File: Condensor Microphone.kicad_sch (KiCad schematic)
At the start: 13 parts, among them J16 Conn_01x02, U2 MAX4466EXK_T

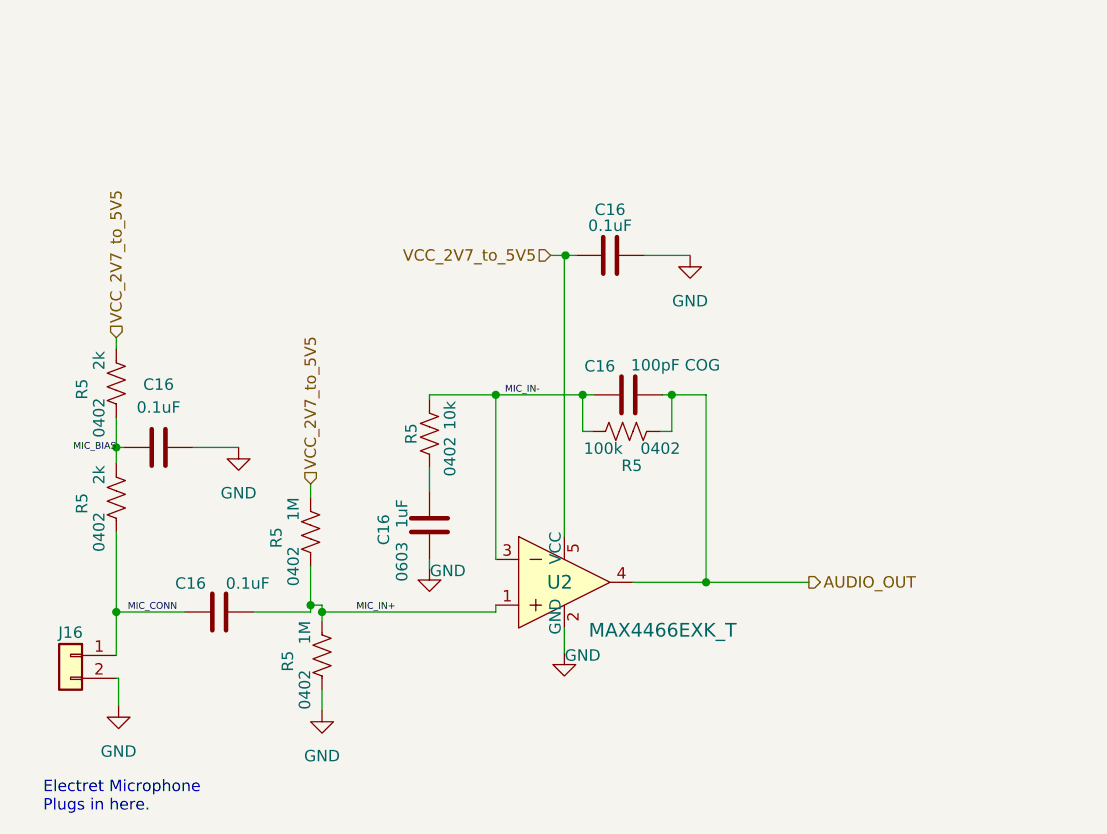
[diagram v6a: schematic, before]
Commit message: updated parts with those available on jlpcb
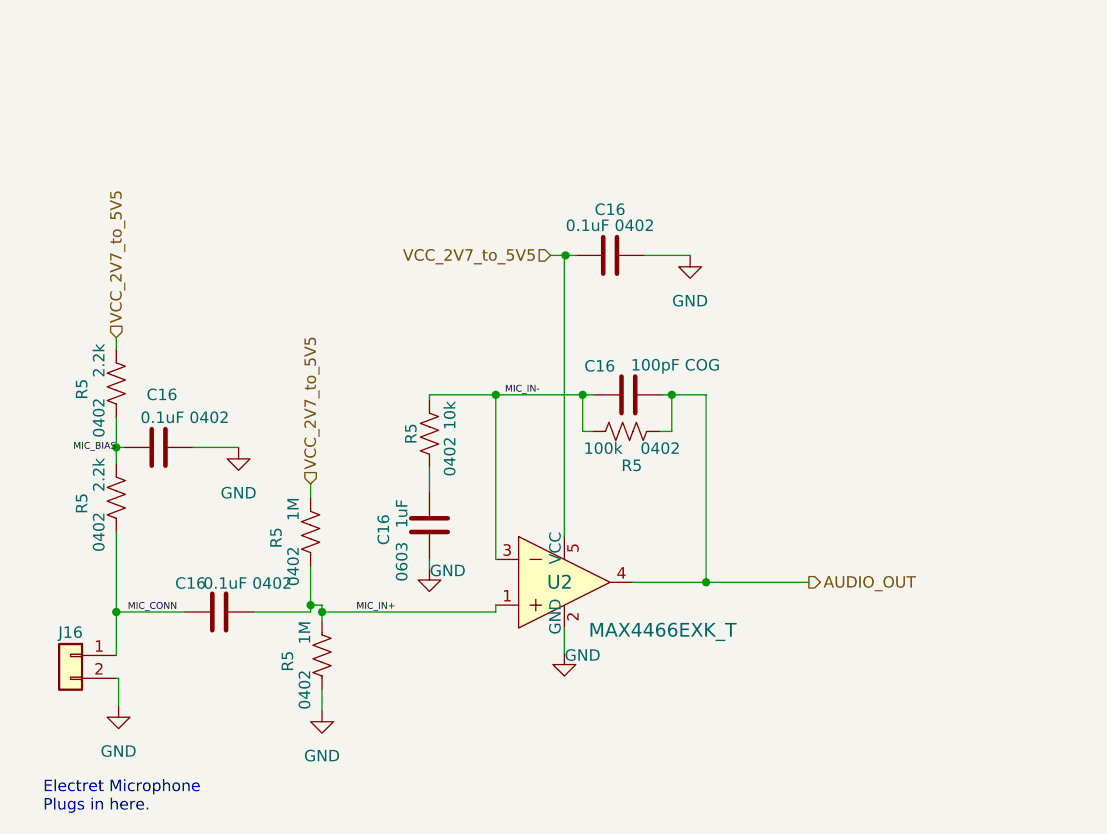
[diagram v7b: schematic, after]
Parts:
- C16: value 0.1uF -> 0.1uF 0402
- R5: value 2k -> 2.2k
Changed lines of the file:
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@@
       (effects (font (size 1.27 1.27)))
     )
-    (property "Value" "0.1uF" (at 155.194 61.214 90)
+    (property "Value" "0.1uF 0402" (at 155.194 61.214 90)
       (effects (font (size 1.27 1.27)))
     )
@@
       (effects (font (size 1.27 1.27)))
     )
-    (property "Value" "0.1uF" (at 114.935 100.965 90)
+    (property "Value" "0.1uF 0402" (at 114.935 100.965 90)
       (effects (font (size 1.27 1.27)))
     )
@@
       (effects (font (size 1.27 1.27)))
     )
-    (property "Value" "2k" (at 98.425 88.9 90)
+    (property "Value" "2.2k" (at 98.425 88.9 90)
       (effects (font (size 1.27 1.27)))
     )
@@
       (effects (font (size 1.27 1.27)))
     )
-    (property "Value" "2k" (at 98.425 76.2 90)
+    (property "Value" "2.2k" (at 98.425 76.2 90)
       (effects (font (size 1.27 1.27)))
     )
@@
   )
   (symbol (lib_id "Device:C") (at 105.029 85.852 90) (unit 1)
-    (in_bom yes) (on_board yes) (dnp no) (fields_autoplaced)
-    (property "Reference" "C16" (at 105.029 78.867 90)
-      (effects (font (size 1.27 1.27)))
-    )
-    (property "Value" "0.1uF" (at 105.029 81.407 90)
-      (effects (font (size 1.27 1.27)))
-    )
+    (in_bom yes) (on_board yes) (dnp no)
+    (property "Reference" "C16" (at 105.41 80.01 90)
+      (effects (font (size 1.27 1.27)))
+    )
+    (property "Value" "0.1uF 0402" (at 107.95 82.55 90)
+      (effects (font (size 1.27 1.27)))
+    )

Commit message: Moved everything to the top side
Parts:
- C16: footprint Capacitor_SMD:C_0402_1005Metric -> Capacitor_SMD:C_0603_1608Metric
- R5: footprint Resistor_SMD:R_0402_1005Metric -> Resistor_SMD:R_0603_1608Metric
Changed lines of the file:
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@@
       (effects (font (size 1.27 1.27)))
     )
-    (property "Footprint" "Capacitor_SMD:C_0402_1005Metric" (at 159.004 63.5508 0)
+    (property "Footprint" "Capacitor_SMD:C_0603_1608Metric" (at 159.004 63.5508 0)
       (effects (font (size 1.27 1.27)) hide)
     )
@@
       (effects (font (size 1.27 1.27)))
     )
-    (property "Footprint" "Resistor_SMD:R_0402_1005Metric" (at 122.174 108.712 90)
+    (property "Footprint" "Resistor_SMD:R_0603_1608Metric" (at 122.174 108.712 90)
       (effects (font (size 1.27 1.27)) hide)
     )
@@
       (effects (font (size 1.27 1.27)))
     )
-    (property "Footprint" "Resistor_SMD:R_0402_1005Metric" (at 134.112 84.074 90)
+    (property "Footprint" "Resistor_SMD:R_0603_1608Metric" (at 134.112 84.074 90)
       (effects (font (size 1.27 1.27)) hide)
     )
@@
       (effects (font (size 1.27 1.27)))
     )
-    (property "Footprint" "Resistor_SMD:R_0402_1005Metric" (at 156.718 85.09 90)
+    (property "Footprint" "Resistor_SMD:R_0603_1608Metric" (at 156.718 85.09 90)
       (effects (font (size 1.27 1.27)) hide)
     )
@@
       (effects (font (size 1.27 1.27)))
     )
-    (property "Footprint" "Capacitor_SMD:C_0402_1005Metric" (at 115.57 103.1748 0)
+    (property "Footprint" "Capacitor_SMD:C_0603_1608Metric" (at 115.57 103.1748 0)
       (effects (font (size 1.27 1.27)) hide)
     )
@@
       (effects (font (size 1.27 1.27)))
     )
-    (property "Footprint" "Resistor_SMD:R_0402_1005Metric" (at 99.314 91.186 90)
+    (property "Footprint" "Resistor_SMD:R_0603_1608Metric" (at 99.314 91.186 90)
       (effects (font (size 1.27 1.27)) hide)
     )
@@
       (effects (font (size 1.27 1.27)))
     )
-    (property "Footprint" "Resistor_SMD:R_0402_1005Metric" (at 120.904 94.996 90)
+    (property "Footprint" "Resistor_SMD:R_0603_1608Metric" (at 120.904 94.996 90)
       (effects (font (size 1.27 1.27)) hide)
     )
@@
       (effects (font (size 1.27 1.27)))
     )
-    (property "Footprint" "Resistor_SMD:R_0402_1005Metric" (at 99.314 78.486 90)
+    (property "Footprint" "Resistor_SMD:R_0603_1608Metric" (at 99.314 78.486 90)
       (effects (font (size 1.27 1.27)) hide)
     )
@@
       (effects (font (size 1.27 1.27)))
     )
-    (property "Footprint" "Capacitor_SMD:C_0402_1005Metric" (at 161.036 79.0448 0)
+    (property "Footprint" "Capacitor_SMD:C_0603_1608Metric" (at 161.036 79.0448 0)
       (effects (font (size 1.27 1.27)) hide)
     )
@@
       (effects (font (size 1.27 1.27)))
     )
-    (property "Footprint" "Capacitor_SMD:C_0402_1005Metric" (at 108.839 84.8868 0)
-      (effects (font (size 1.27 1.27)) hide)
-    )
+    (property "Footprint" "Capacitor_SMD:C_0603_1608Metric" (at 108.839 84.8868 0)
+      (effects (font (size 1.27 1.27)) hide)
+    )
